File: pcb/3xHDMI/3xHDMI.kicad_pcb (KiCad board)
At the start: 4 copper layers, 100 x 35.5 mm, 99 parts, among them J1 HDMI0-OUT, J10 SERIAL, J11 Conn_01x02, J2 Conn_01x02, J3 HDMI1-OUT, J4 HDMI2-INOUT, J5 KH-TYPE-C-16P, J6 POWER_O, J7 DATA3, J8 DATA2, J9 DATA1, P1 Header-Female-2.54_1x8, Q1 AO3400, Q2 AO3400, Q3 AO3400, Q4 AO3400, Q5 AO3400, Q6 AO3400, Q7 AO3400, Q8 AO3400, Q9 AO3400, SW1 KEY, SW2 KEY, SW3 KEY, SW4 KEY, SW5 KEY, SW6 KEY, U1 CH340G, U2 AMS1117-3.3, X1 12MHz

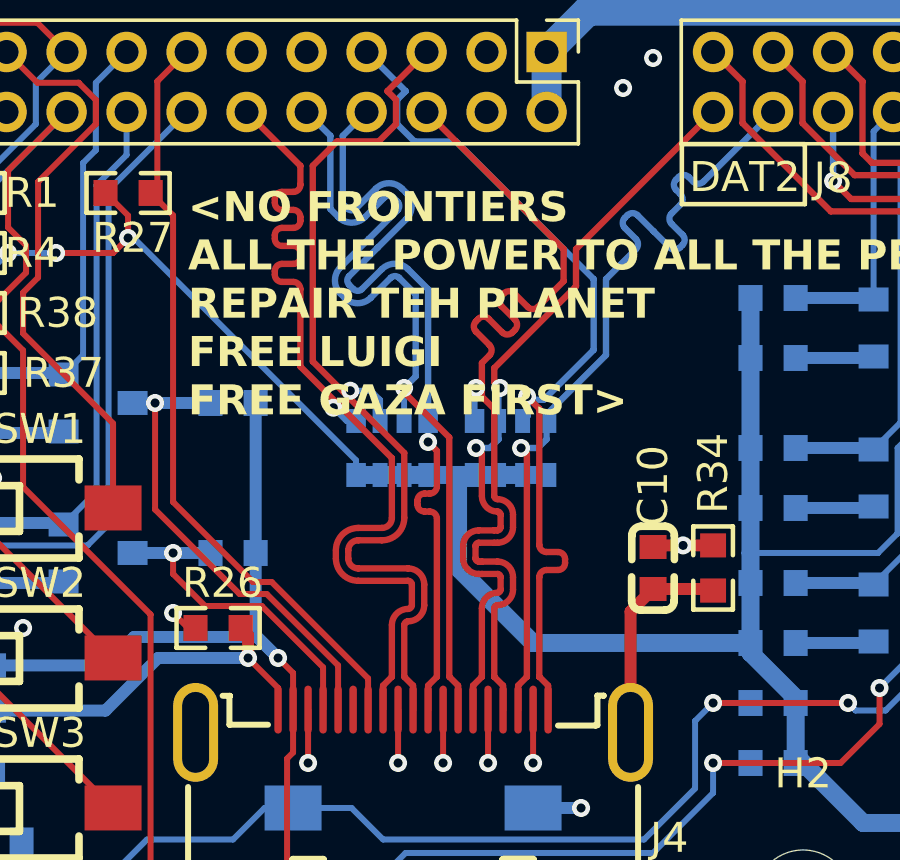
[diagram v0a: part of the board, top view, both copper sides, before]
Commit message: Update stack up and some other clean up
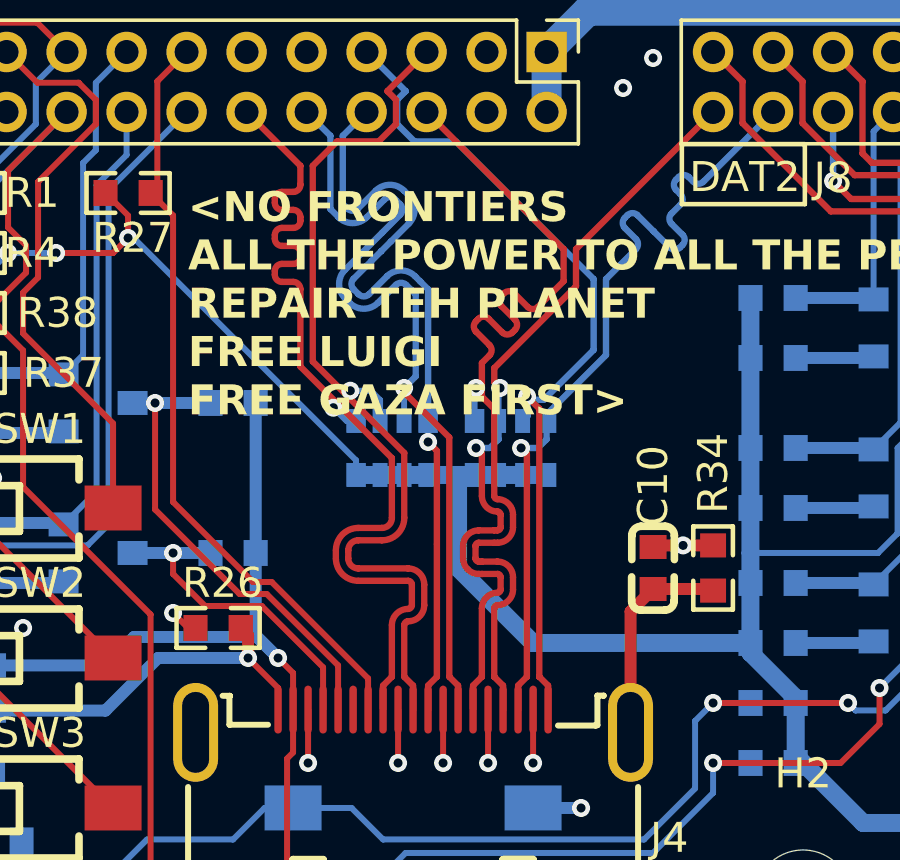
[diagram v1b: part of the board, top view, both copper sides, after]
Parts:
- C10, C11, C12: value 103 -> 103n
- C3, C7, C9: value 104 -> 104n
- C4, C5: value 22P -> 22p
- C6, C8: value 106 -> 106n
- J3: value HDMI1-OUT -> HDMI1-INOUT
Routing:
- net /HDMI2_D2+: track 29.8 -> 28.5 mm
- net /HDMI2_D0-: track 29.1 -> 28.1 mm
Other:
- board text added: "3 stars, 2 freedoms, 1 word, Octonion, 2^{3}, Reborn from/for creatrices"
- board text removed: "0"
- board text removed: "0 mm"
- board text removed: "0.0000 mm / 0.0000 mm"
- board text removed: "0.01 mm"
- board text removed: "0.02"
- board text removed: "0.03 mm"
- board text removed: "0.035 mm"
- board text removed: "0.203 mm"
- board text removed: "0.3000 mm"
- board text removed: "1"
- board text removed: "1.03 mm"
- board text removed: "1.5860 mm"
- board text removed: "100.0066 mm x 35.5032 mm"
- board text removed: "3.3"
- board text removed: "4"
- board text removed: "4.4"
- board text removed: "4.6"
- board text removed: "B.Cu"
- board text removed: "B.Mask"
- board text removed: "B.Paste"
- board text removed: "B.Silkscreen"
- board text removed: "BOARD CHARACTERISTICS"
- board text removed: "Board Thickness:"
- board text removed: "Board overall dimensions:"
- board text removed: "Bottom Silk Screen"
- board text removed: "Bottom Solder Mask"
- board text removed: "Bottom Solder Paste"
- board text removed: "Castellated pads:"
- board text removed: "Color"
- board text removed: "Copper Finish:"
- board text removed: "Copper Layer Count:"
- board text removed: "Dielectric 1"
- board text removed: "Dielectric 2"
- board text removed: "Dielectric 3"
- board text removed: "ENIG"
- board text removed: "Edge card connectors:"
- board text removed: "Epsilon R"
- board text removed: "F.Cu"
- board text removed: "F.Mask"
- board text removed: "F.Paste"
- board text removed: "F.Silkscreen"
- board text removed: "FR4"
- board text removed: "Impedance Control:"
- board text removed: "In1.Cu"
- board text removed: "In2.Cu"
- board text removed: "Layer Name"
- board text removed: "Loss Tangent"
- board text removed: "Material"
- board text removed: "Min hole diameter:"
- board text removed: "Min track/spacing:"
- board text removed: "No"
- board text removed: "Not specified"
- board text removed: "Plated Board Edge:"
- board text removed: "Thickness (mm)"
- board text removed: "Top Silk Screen"
- board text removed: "Top Solder Mask"
- board text removed: "Top Solder Paste"
- board text removed: "Type"
- board text removed: "Yes"
- board text removed: "copper"
- board text removed: "core"
- board text removed: "prepreg"
